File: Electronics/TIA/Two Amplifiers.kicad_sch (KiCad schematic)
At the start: 8 parts, among them U2 ${SIM.PARAMS}

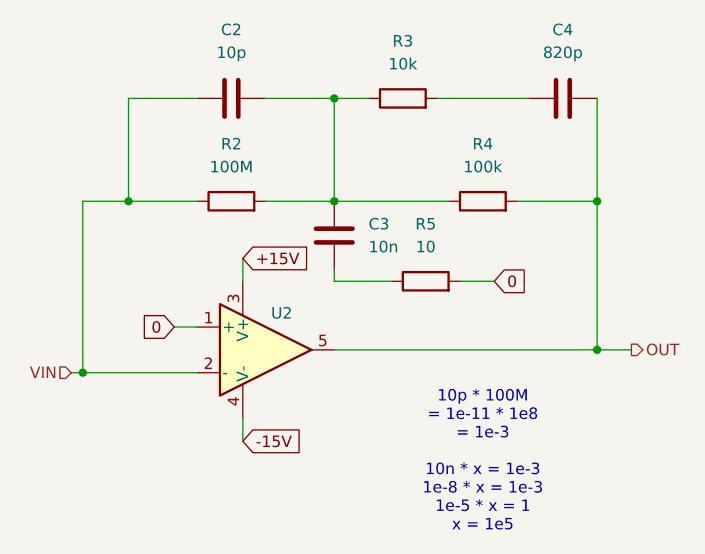
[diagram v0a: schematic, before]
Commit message: Create a robust TIA design following the requirements
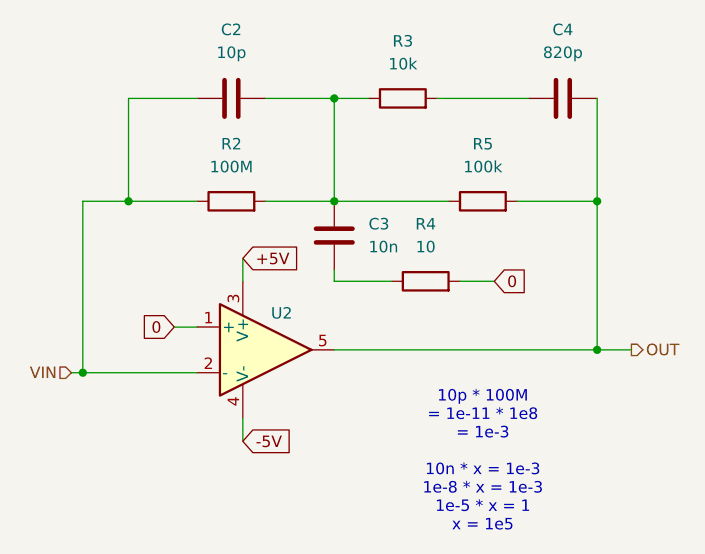
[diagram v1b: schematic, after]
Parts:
- renumbered R5 to R4, R4 to R5
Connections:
- net +15V renamed +5V
- net -15V renamed -5V
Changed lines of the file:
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@@
 		)
 	)
-	(global_label "-15V"
+	(global_label "-5V"
 		(shape input)
 		(at 173.99 128.27 0)
@@
 		)
 		(property "Intersheetrefs" "${INTERSHEET_REFS}"
-			(at 182.0552 128.27 0)
+			(at 180.8457 128.27 0)
 			(hide yes)
 			(show_name no)
@@
 		)
 	)
-	(global_label "+15V"
+	(global_label "+5V"
 		(shape input)
 		(at 173.99 107.95 0)
@@
 		)
 		(property "Intersheetrefs" "${INTERSHEET_REFS}"
-			(at 182.0552 107.95 0)
+			(at 180.8457 107.95 0)
 			(hide yes)
 			(show_name no)
@@
 		(dnp no)
 		(fields_autoplaced yes)
-		(property "Reference" "R4"
+		(property "Reference" "R5"
 			(at 200.66 95.25 90)
 			(show_name no)
@@
 			(project "TIA"
 				(path "/54290178-5b03-4b9d-bd2e-fef7d018d5b4/06543960-6df5-427c-bcfd-4b08397f7203"
-					(reference "R4")
+					(reference "R5")
 					(unit 1)
 				)
@@
 		(dnp no)
 		(fields_autoplaced yes)
-		(property "Reference" "R5"
+		(property "Reference" "R4"
 			(at 194.31 104.14 90)
 			(show_name no)
@@
 			(project "TIA"
 				(path "/54290178-5b03-4b9d-bd2e-fef7d018d5b4/06543960-6df5-427c-bcfd-4b08397f7203"
-					(reference "R5")
+					(reference "R4")
 					(unit 1)
 				)
